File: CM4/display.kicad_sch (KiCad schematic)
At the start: 1 part

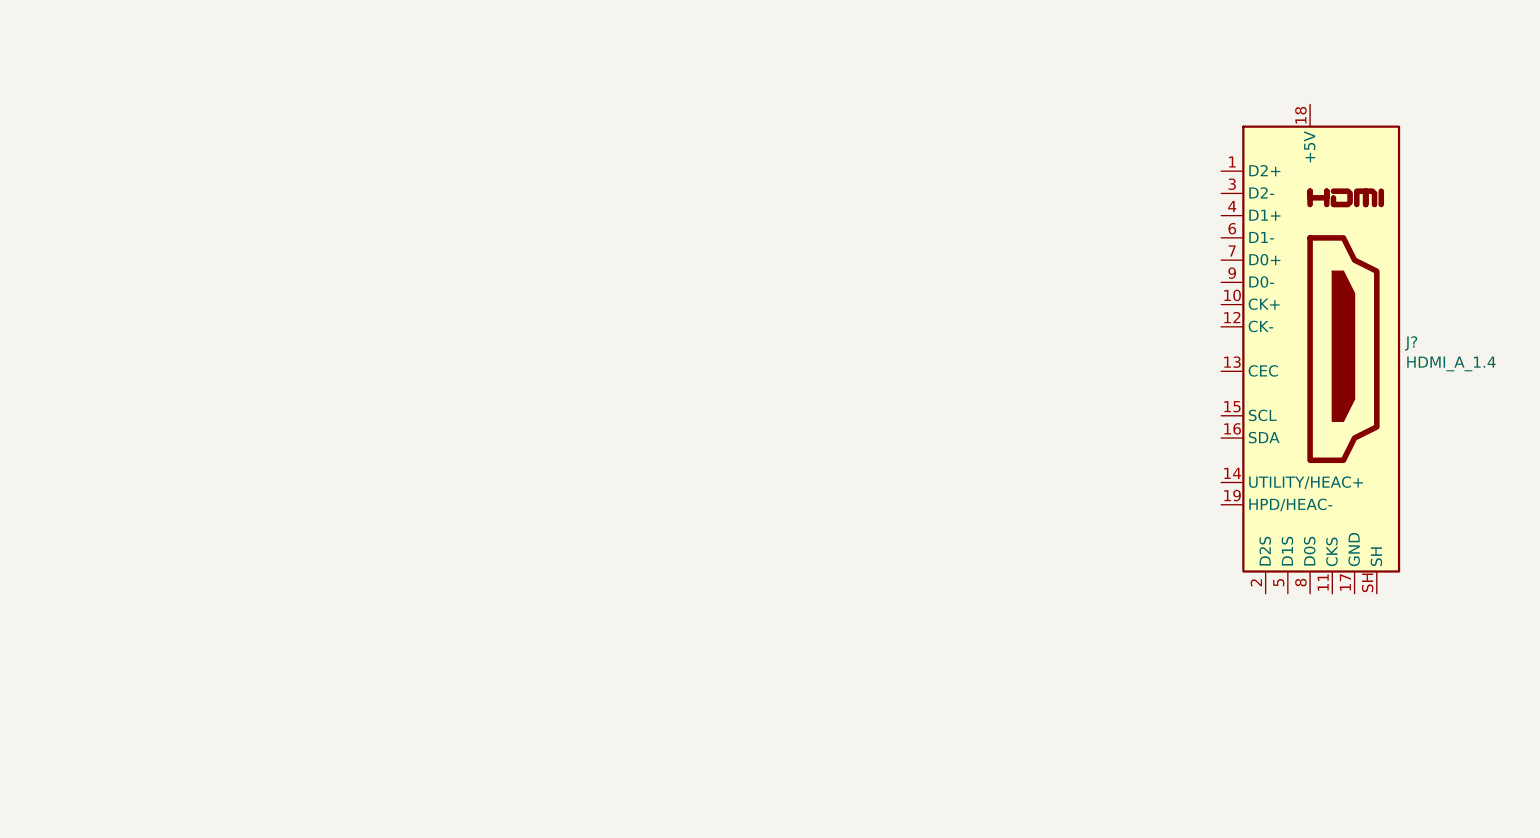
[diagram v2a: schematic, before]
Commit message: adding hdmi connector
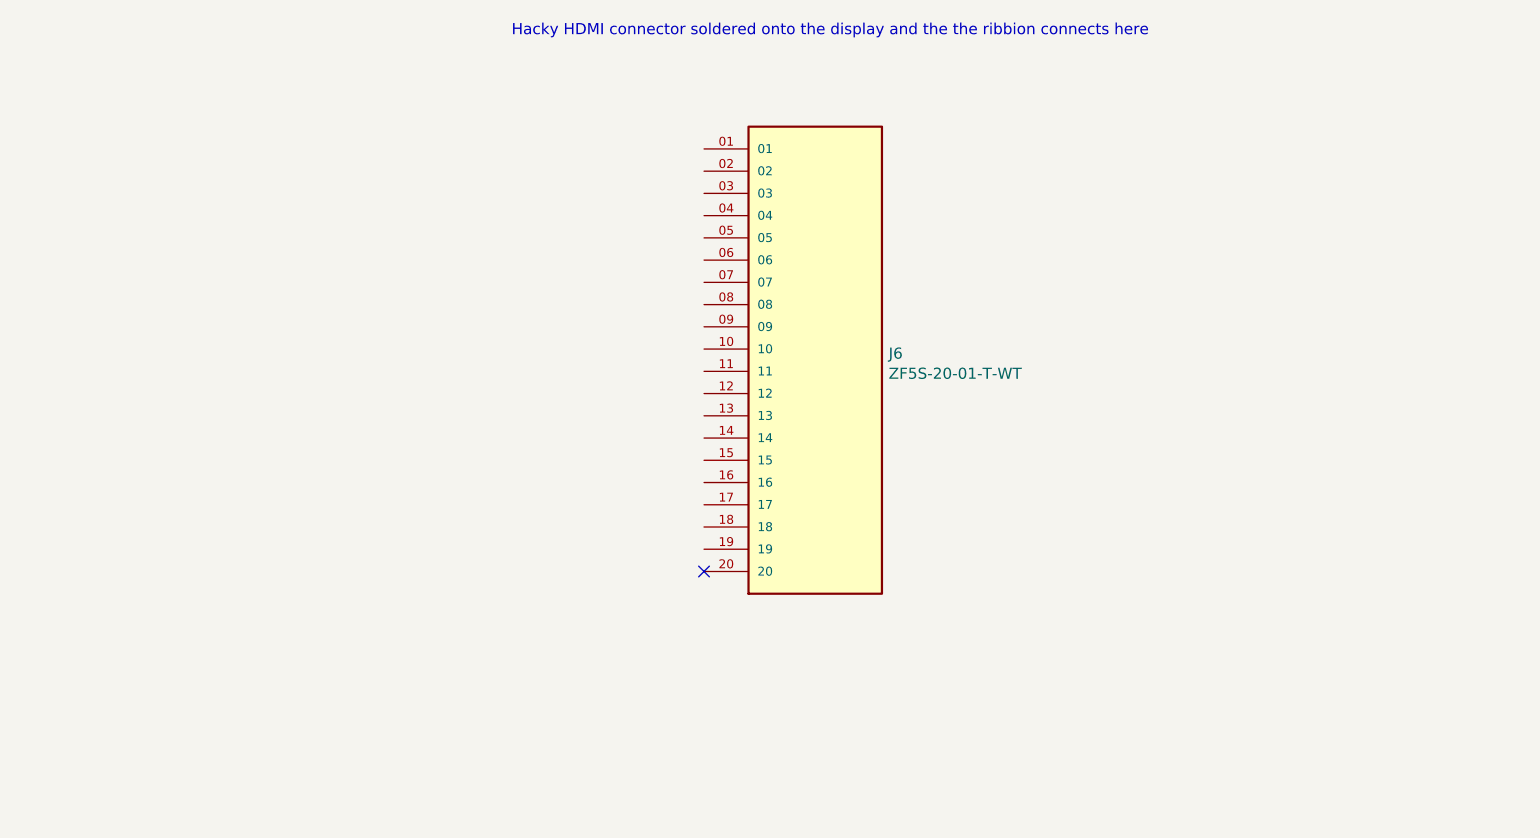
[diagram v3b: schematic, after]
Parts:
- removed J?: HDMI_A_1.4, symbol Connector:HDMI_A_1.4
- added J6: ZF5S-20-01-T-WT, SAMTEC_ZF5S-20-01-T-WT, symbol ZF5S-20-01-T-WT:ZF5S-20-01-T-WT
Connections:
- no-connect marks 0 -> 1
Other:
- note added: "Hacky HDMI connector soldered onto the display and the the ribbion connects here"
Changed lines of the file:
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@@
 (kicad_sch (version 20210126) (generator eeschema)
   (paper "A4")
-  (symbol (lib_id "Connector:HDMI_A_1.4") (at 219.71 96.52 0) (unit 1)
+  (no_connect (at 150.495 121.92))
+  (text "Hacky HDMI connector soldered onto the display and the the ribbion connects here"
+    (at 201.295 60.96 0)
+    (effects (font (size 1.27 1.27)) (justify right bottom))
+  )
+  (symbol (lib_id "ZF5S-20-01-T-WT:ZF5S-20-01-T-WT") (at 163.195 96.52 0) (unit 1)
     (in_bom yes) (on_board yes)
-    (property "Reference" "J?" (id 0) (at 230.6321 95.7591 0)
+    (property "Reference" "J6" (id 0) (at 171.5771 97.0291 0)
       (effects (font (size 1.27 1.27)) (justify left))
     )
-    (property "Value" "HDMI_A_1.4" (id 1) (at 230.6321 98.0578 0)
+    (property "Value" "ZF5S-20-01-T-WT" (id 1) (at 171.5771 99.3278 0)
       (effects (font (size 1.27 1.27)) (justify left))
     )
-    (property "Footprint" "" (id 2) (at 220.345 96.52 0)
-      (effects (font (size 1.27 1.27)) hide)
+    (property "Footprint" "SAMTEC_ZF5S-20-01-T-WT" (id 2) (at 163.195 96.52 0)
+      (effects (font (size 1.27 1.27)) (justify left bottom) hide)
     )
-    (property "Datasheet" "https://en.wikipedia.org/wiki/HDMI" (id 3) (at 220.345 96.52 0)
-      (effects (font (size 1.27 1.27)) hide)
+    (property "Datasheet" "" (id 3) (at 163.195 96.52 0)
+      (effects (font (size 1.27 1.27)) (justify left bottom) hide)
     )
-    (pin "1")
+    (property "MANUFACTURER" "SAMTEC" (id 4) (at 163.195 96.52 0)
+      (effects (font (size 1.27 1.27)) (justify left bottom) hide)
+    )
+    (pin "01")
+    (pin "02")
+    (pin "03")
+    (pin "04")
+    (pin "05")
+    (pin "06")
+    (pin "07")
+    (pin "08")
+    (pin "09")
     (pin "10")
     (pin "11")
@@
     (pin "18")
     (pin "19")
-    (pin "2")
-    (pin "3")
-    (pin "4")
-    (pin "5")
-    (pin "6")
-    (pin "7")
-    (pin "8")
-    (pin "9")
-    (pin "SH")
+    (pin "20")
   )
 )

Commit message: PrepedHDMIConnections
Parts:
- removed J6: ZF5S-20-01-T-WT, SAMTEC_ZF5S-20-01-T-WT, symbol ZF5S-20-01-T-WT:ZF5S-20-01-T-WT
- added J?: ZF5S-20-01-T-WT, SAMTEC_ZF5S-20-01-T-WT, symbol ZF5S-20-01-T-WT:ZF5S-20-01-T-WT
- added JP10, JP11, JP12, JP13, JP14, JP15, JP16, JP17, JP18, JP19, JP20, JP21, JP22, JP23, JP5, JP6, JP7, JP8, JP9: SolderJumper_2_Bridged, Jumper:SolderJumper-2_P1.3mm_Bridged_Pad1.0x1.5mm, symbol Jumper:SolderJumper_2_Bridged
- added JP24: SolderJumper_2_Bridged, symbol Jumper:SolderJumper_2_Bridged
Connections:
- new net: J?.04, JP8.2 (B)
- new net: J?.01, JP5.2 (B)
- new net: J?.02, JP6.2 (B)
- new net: J?.03, JP7.2 (B)
- new net: J?.05, JP9.2 (B)
- new net: J?.06, JP10.2 (B)
- new net: J?.07, JP11.2 (B)
- new net: J?.08, JP12.2 (B)
- new net: J?.09, JP13.2 (B)
- new net: J?.10, JP14.2 (B)
- new net: J?.11, JP15.2 (B)
- new net: J?.12, JP16.2 (B)
- new net: J?.13, JP17.2 (B)
- new net: J?.14, JP18.2 (B)
- new net: J?.15, JP19.2 (B)
- new net: J?.16, JP20.2 (B)
- new net: J?.17, JP21.2 (B)
- new net: J?.18, JP22.2 (B)
- new net: J?.19, JP23.2 (B)
- new net: J?.20, JP24.2 (B)
- new net GND: JP12.1 (A), JP15.1 (A), JP24.1 (A), JP6.1 (A), JP9.1 (A)
- new net HDMI0_+5V: JP22.1 (A)
- new net HDMI0_CEC: JP17.1 (A)
- new net HDMI0_CK_N: JP16.1 (A)
- new net HDMI0_CK_P: JP14.1 (A)
- new net HDMI0_HOTPLUG: JP23.1 (A)
- new net HDMI0_TX0_N: JP13.1 (A)
- new net HDMI0_TX0_P: JP11.1 (A)
- new net HDMI0_TX1_N: JP10.1 (A)
- new net HDMI0_TX1_P: JP8.1 (A)
- new net HDMI0_TX2_N: JP7.1 (A)
- new net HDMI0_TX2_P: JP5.1 (A)
- no-connect marks 1 -> 4

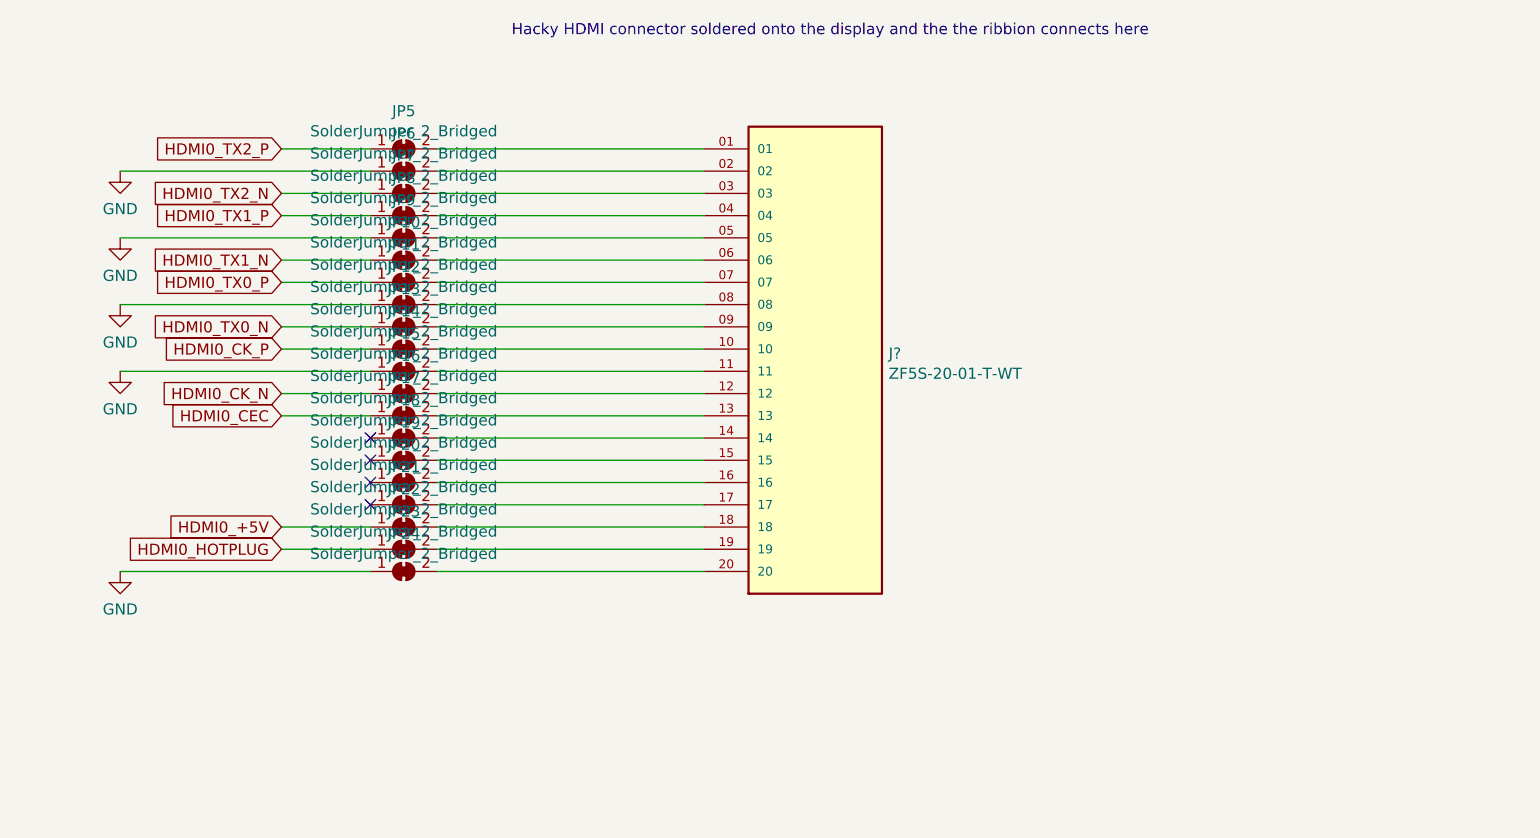
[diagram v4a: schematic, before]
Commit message: Removed Jumpers and just doing hdmi the right way the first time, this wont bite me in the butt
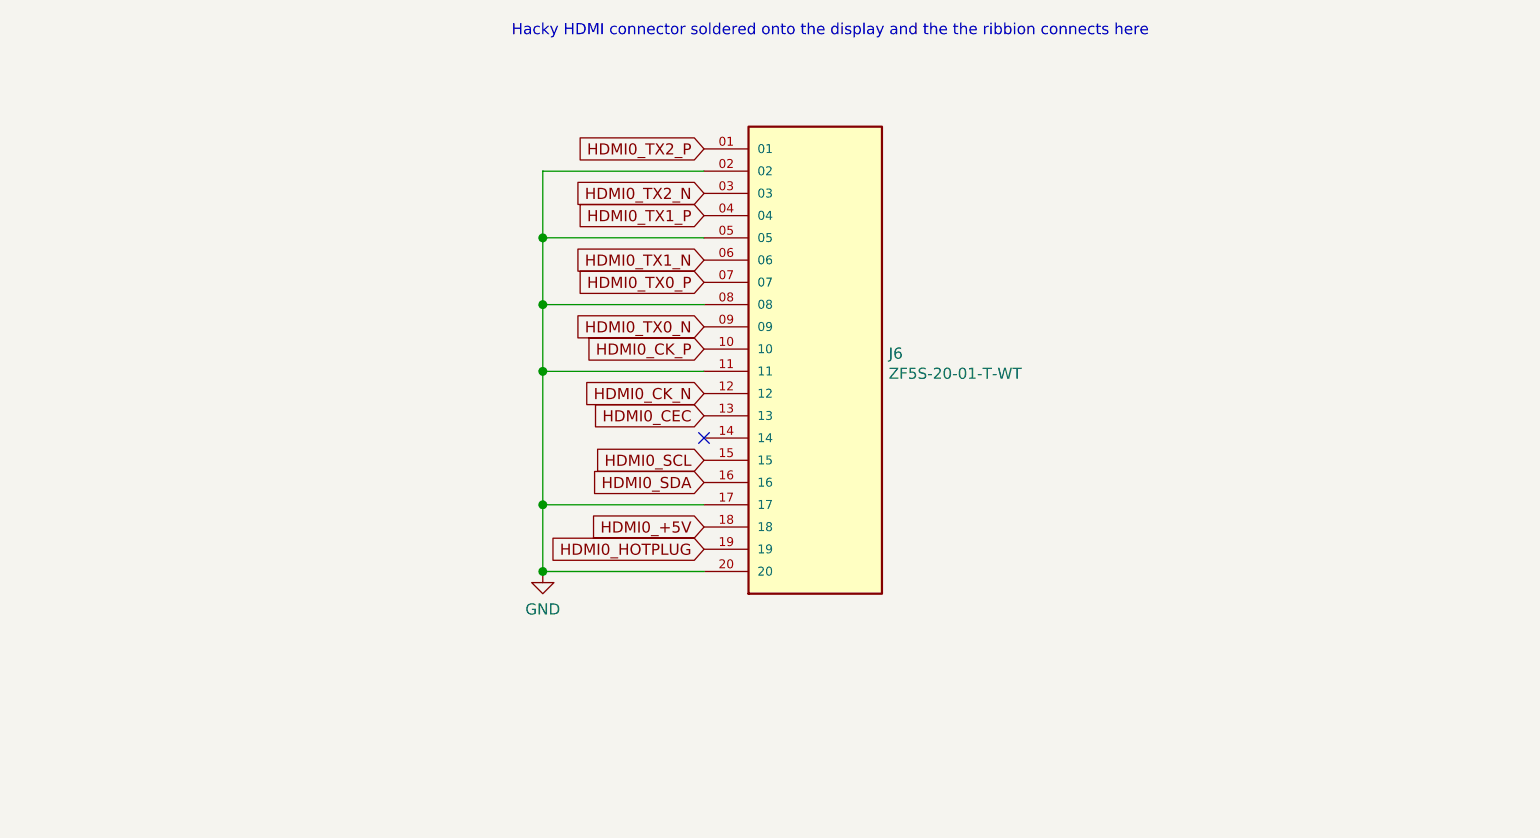
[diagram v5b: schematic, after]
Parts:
- removed JP10, JP11, JP12, JP13, JP14, JP15, JP16, JP17, JP18, JP19, JP20, JP21, JP22, JP23, JP5, JP6, JP7, JP8, JP9: SolderJumper_2_Bridged, Jumper:SolderJumper-2_P1.3mm_Bridged_Pad1.0x1.5mm, symbol Jumper:SolderJumper_2_Bridged
- removed JP24: SolderJumper_2_Bridged, symbol Jumper:SolderJumper_2_Bridged
- gave numbers to parts that had none: 1
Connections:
- net GND: now also J6.02, J6.05, J6.08, J6.11, J6.17, J6.20
- net HDMI0_+5V: now also J6.18
- net HDMI0_CEC: now also J6.13
- net HDMI0_CK_N: now also J6.12
- net HDMI0_CK_P: now also J6.10
- net HDMI0_HOTPLUG: now also J6.19
- net HDMI0_TX0_N: now also J6.09
- net HDMI0_TX0_P: now also J6.07
- net HDMI0_TX1_N: now also J6.06
- net HDMI0_TX1_P: now also J6.04
- net HDMI0_TX2_N: now also J6.03
- net HDMI0_TX2_P: now also J6.01
- net HDMI0_SCL: now reaches J6.15
- net HDMI0_SDA: now reaches J6.16
- no-connect marks 4 -> 1

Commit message: Compleated REV001
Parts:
- added J8: Conn_01x02_Male, Connector_PinHeader_1.00mm:PinHeader_1x02_P1.00mm_Vertical, symbol Connector:Conn_01x02_Male
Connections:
- net GND: now also J8.2 (Pin_2)
- new net relay_no_b: J8.1 (Pin_1)
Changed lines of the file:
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@@
     (effects (font (size 1.27 1.27)) (justify right bottom))
+  )
+  (global_label "relay_no_b" (shape input) (at 99.0092 142.1892 0)
+    (effects (font (size 1.27 1.27)) (justify left))
+    (property "Intersheet References" "${INTERSHEET_REFS}" (id 0) (at 111.4613 142.1098 0)
+      (effects (font (size 1.27 1.27)) (justify left) hide)
+    )
   )
   (global_label "HDMI0_TX2_P" (shape input) (at 150.495 73.66 180)
@@
     )
   )
+  (symbol (lib_id "power:GND") (at 99.0092 144.7292 0) (unit 1)
+    (in_bom yes) (on_board yes)
+    (property "Reference" "#PWR0150" (id 0) (at 99.0092 151.0792 0)
+      (effects (font (size 1.27 1.27)) hide)
+    )
+    (property "Value" "GND" (id 1) (at 99.0092 149.0536 0))
+    (property "Footprint" "" (id 2) (at 99.0092 144.7292 0)
+      (effects (font (size 1.27 1.27)) hide)
+    )
+    (property "Datasheet" "" (id 3) (at 99.0092 144.7292 0)
+      (effects (font (size 1.27 1.27)) hide)
+    )
+    (pin "1")
+  )
   (symbol (lib_id "power:GND") (at 132.08 121.92 0) (unit 1)
     (in_bom yes) (on_board yes)
@@
     (pin "1")
   )
+  (symbol (lib_id "Connector:Conn_01x02_Male") (at 93.9292 142.1892 0) (unit 1)
+    (in_bom yes) (on_board yes)
+    (property "Reference" "J8" (id 0) (at 96.6216 138.502 0))
+    (property "Value" "Conn_01x02_Male" (id 1) (at 96.5708 136.4319 0))
+    (property "Footprint" "Connector_PinHeader_1.00mm:PinHeader_1x02_P1.00mm_Vertical" (id 2) (at 93.9292 142.1892 0)
+      (effects (font (size 1.27 1.27)) hide)
+    )
+    (property "Datasheet" "~" (id 3) (at 93.9292 142.1892 0)
+      (effects (font (size 1.27 1.27)) hide)
+    )
+    (pin "1")
+    (pin "2")
+  )
   (symbol (lib_id "ZF5S-20-01-T-WT:ZF5S-20-01-T-WT") (at 163.195 96.52 0) (unit 1)
